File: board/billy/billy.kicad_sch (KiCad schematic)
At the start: 65 parts, among them J1 Screw_Terminal_01x02, J10 Screw_Terminal_01x02, J11 Screw_Terminal_01x02, J2 Conn_01x06, J3 Screw_Terminal_01x02, J4 Screw_Terminal_01x02, J5 USB_C_Receptacle_USB2.0_16P, J6 Screw_Terminal_01x02, J8 Screw_Terminal_01x03, J9 Screw_Terminal_01x02, Q1 AO3400A, Q2 AO3400A, Q3 AO3400A, SW1 TS-1088-AR02016, U1 ESP32-S3-WROOM-1, U2 DRV8833PWP, U3 MAX98357A, U4 DRV8833PWP

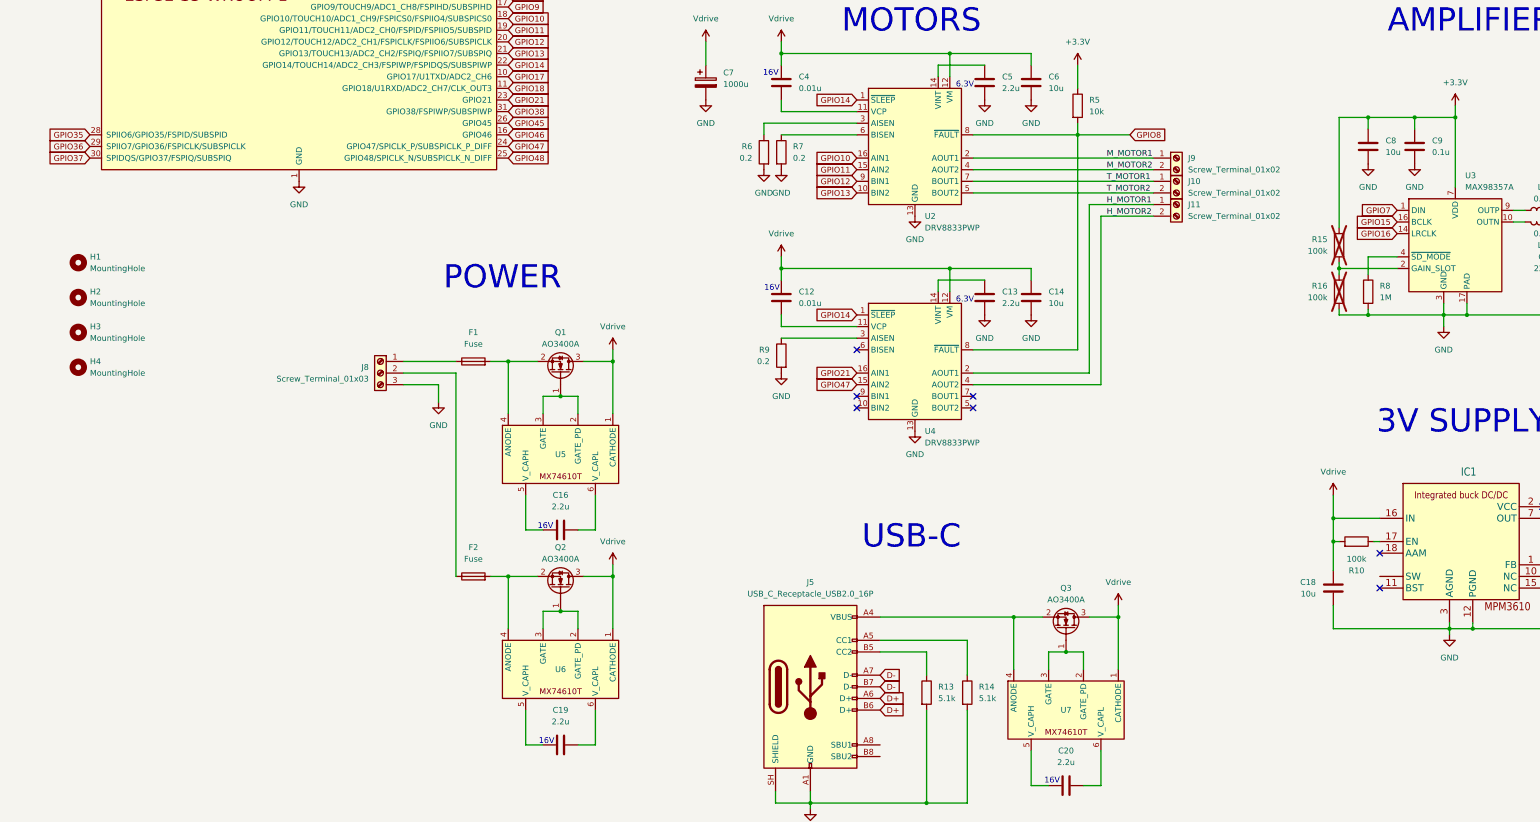
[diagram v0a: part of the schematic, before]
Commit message: Add gated status LED (WS2812, low-side FET VDD switch) to schematic/board and firmware
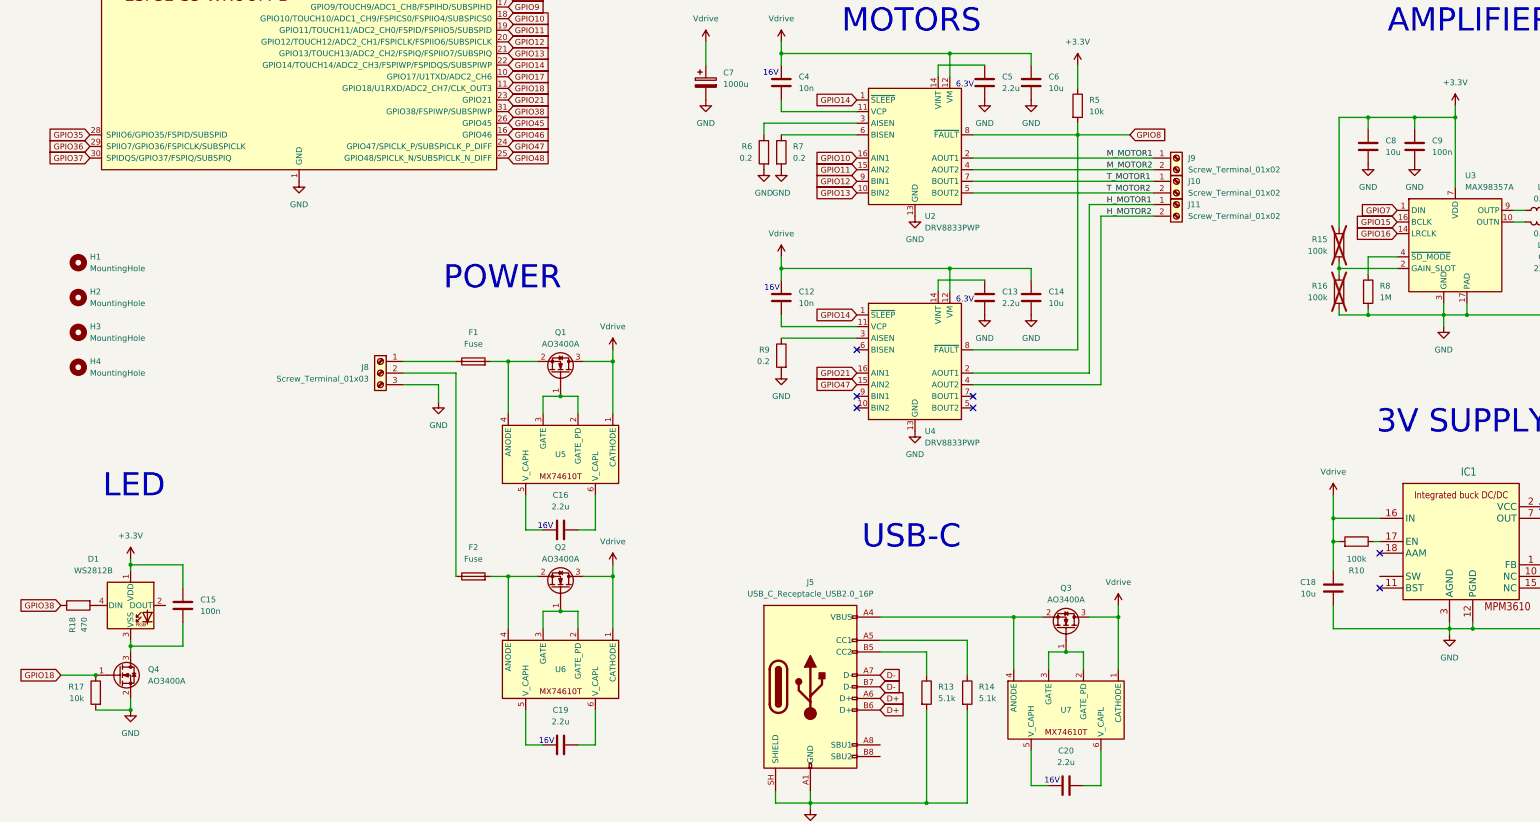
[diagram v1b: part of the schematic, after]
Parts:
- added C15: 100n, Capacitor_SMD:C_0402_1005Metric, symbol Device:C
- added D1: WS2812B, LED_SMD:LED_WS2812B_PLCC4_5.0x5.0mm_P3.2mm, symbol LED:WS2812B
- added Q4: AO3400A, Package_TO_SOT_SMD:SOT-23, symbol Transistor_FET:AO3400A
- added R17: 10k, Resistor_SMD:R_0603_1608Metric, symbol Device:R
- added R18: 470, Resistor_SMD:R_0603_1608Metric, symbol Device:R
- C12, C4: value 0.01u -> 10n
- C9: value 0.1u -> 100n
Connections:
- net +3.3V: now also C15.1, D1.1 (VDD)
- net GND: now also Q4.2 (S), R17.2
- net GPIO18: now also Q4.1 (G), R17.1
- net GPIO38: now also R18.1
- new net: C15.2, D1.3 (VSS), Q4.3 (D)
- new net: D1.4 (DIN), R18.2
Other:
- note added: "LED"

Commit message: Complete board layout, assign LCSC part numbers, verify footprints; passes DRC
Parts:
- C1, C2, C3: footprint Capacitor_SMD:C_0603_1608Metric -> Capacitor_SMD:C_0402_1005Metric; LCSC C15849 -> C52923
- C10, C11: footprint Capacitor_SMD:C_0603_1608Metric -> Capacitor_SMD:C_0402_1005Metric; LCSC C15849 -> C1530
- C16, C19, C20: footprint Capacitor_SMD:C_1206_3216Metric -> Capacitor_SMD:C_0402_1005Metric; LCSC C50254 -> C12530
- J1, J10, J11, J3, J4, J6, J9: LCSC (none) -> C918120
- J2: LCSC (none) -> C56816
- J8: LCSC (none) -> C918121
- L1, L2: value 0.15 -> 50m; LCSC (none) -> C14709
- Q1, Q2, Q3, Q4: LCSC (none) -> AO3400A
- R1, R13, R14: LCSC (none) -> C23186
- R10: LCSC (none) -> C25803
- R11: LCSC (none) -> C23242
- R12: LCSC (none) -> C23352
- R15, R16: now left out of the parts list
- R17, R2, R3, R4, R5: LCSC (none) -> C25804
- R18: LCSC (none) -> C23179
- R6, R7, R9: footprint Resistor_SMD:R_0603_1608Metric -> Resistor_SMD:R_1206_3216Metric; LCSC (none) -> C473037
- R8: LCSC (none) -> C22935
- SW1: footprint billy:SW-SMD_L3.9-W3.0-P4.45 -> Button_Switch_SMD:SW_SPST_TS-1088-xR020; LCSC (none) -> C720477
- U1: LCSC (none) -> C2913203
- U2, U4: value DRV8833PWP -> DRV8833PWPR; LCSC (none) -> C50506
- U3: LCSC (none) -> C910544
- U5, U6, U7: LCSC (none) -> C19078229
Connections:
- no-connect marks 8 -> 12

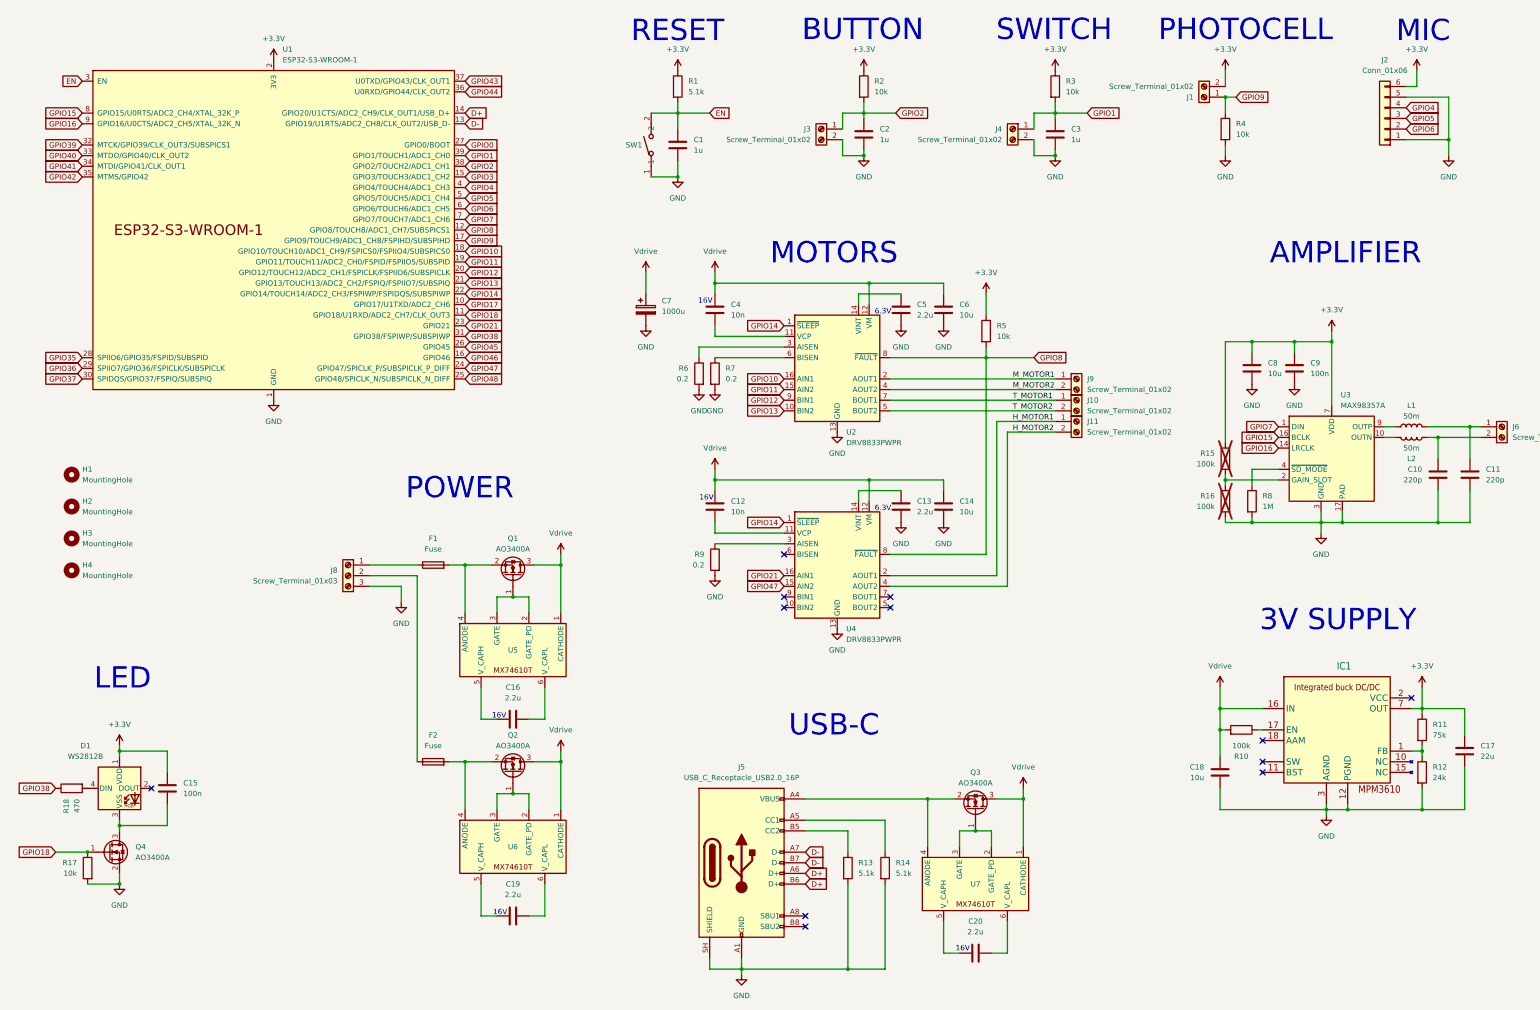
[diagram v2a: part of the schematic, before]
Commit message: Fix some minor ERC and DRC checks
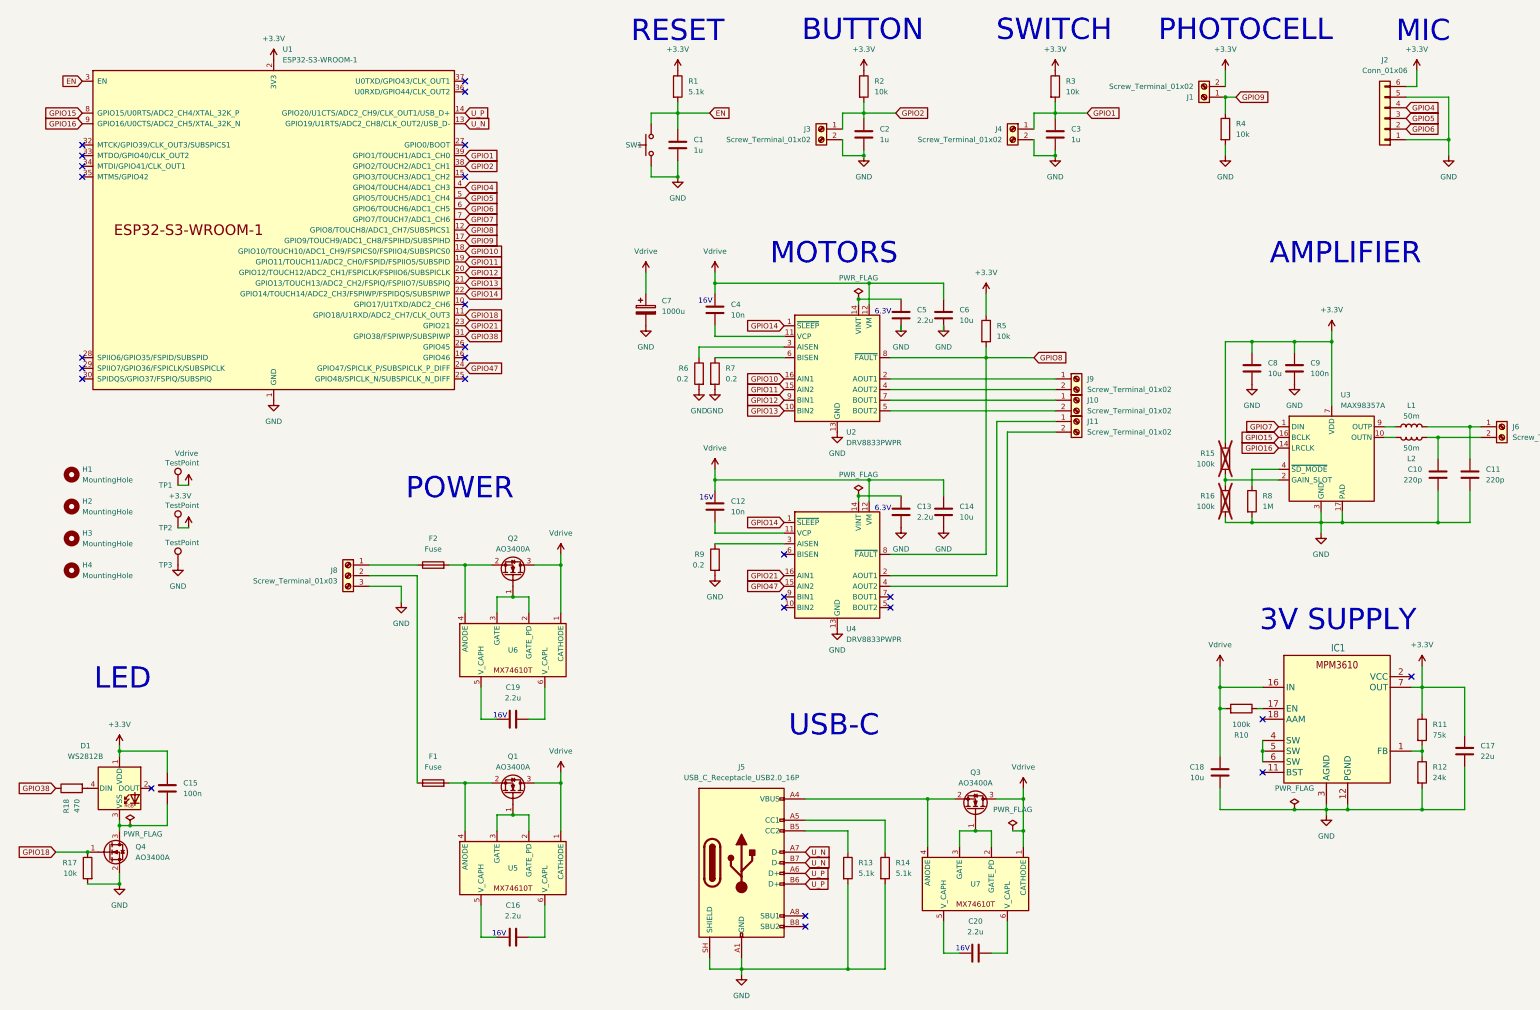
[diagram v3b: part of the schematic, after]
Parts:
- added TP1, TP2, TP3: TestPoint, TestPoint:TestPoint_Pad_1.0x1.0mm, symbol Connector:TestPoint
- SW1: symbol billy:TS-1088-AR02016 -> Switch:SW_Push
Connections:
- net +3.3V: now also TP2.1
- net GND: now also TP3.1
- net Vdrive: now also TP1.1
- net at F1.1: now also J8.2 (Pin_2); no longer J8.1 (Pin_1)
- net at F2.1: now also J8.1 (Pin_1); no longer J8.2 (Pin_2)
- net D+ renamed U_P
- net D- renamed U_N
- net GPIO0: no longer names the net of U1.27 (GPIO0/BOOT)
- net GPIO17: no longer names the net of U1.10 (GPIO17/U1TXD/ADC2_CH6)
- net GPIO3: no longer names the net of U1.15 (GPIO3/TOUCH3/ADC1_CH2)
- net GPIO35: no longer names the net of U1.28 (SPIIO6/GPIO35/FSPID/SUBSPID)
- net GPIO36: no longer names the net of U1.29 (SPIIO7/GPIO36/FSPICLK/SUBSPICLK)
- net GPIO37: no longer names the net of U1.30 (SPIDQS/GPIO37/FSPIQ/SUBSPIQ)
- net GPIO39: no longer names the net of U1.32 (MTCK/GPIO39/CLK_OUT3/SUBSPICS1)
- net GPIO40: no longer names the net of U1.33 (MTDO/GPIO40/CLK_OUT2)
- net GPIO41: no longer names the net of U1.34 (MTDI/GPIO41/CLK_OUT1)
- net GPIO42: no longer names the net of U1.35 (MTMS/GPIO42)
- net GPIO43: no longer names the net of U1.37 (U0TXD/GPIO43/CLK_OUT1)
- net GPIO44: no longer names the net of U1.36 (U0RXD/GPIO44/CLK_OUT2)
- net GPIO45: no longer names the net of U1.26 (GPIO45)
- net GPIO46: no longer names the net of U1.16 (GPIO46)
- net GPIO48: no longer names the net of U1.25 (GPIO48/SPICLK_N/SUBSPICLK_N_DIFF)
- net H_MOTOR1: no longer names the net of J11.1 (Pin_1), U4.2 (AOUT1)
- net H_MOTOR2: no longer names the net of J11.2 (Pin_2), U4.4 (AOUT2)
- net M_MOTOR1: no longer names the net of J9.1 (Pin_1), U2.2 (AOUT1)
- net M_MOTOR2: no longer names the net of J9.2 (Pin_2), U2.4 (AOUT2)
- net T_MOTOR1: no longer names the net of J10.1 (Pin_1), U2.7 (BOUT1)
- net T_MOTOR2: no longer names the net of J10.2 (Pin_2), U2.5 (BOUT2)
- no-connect marks 12 -> 26
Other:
- title: Big Mouth Billy Bass -> Smart Mouth Billy Bass
- moved on the sheet: C13, C14, C16, C19, C5, C6, F1, F2, Q1, Q2, R10, U5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

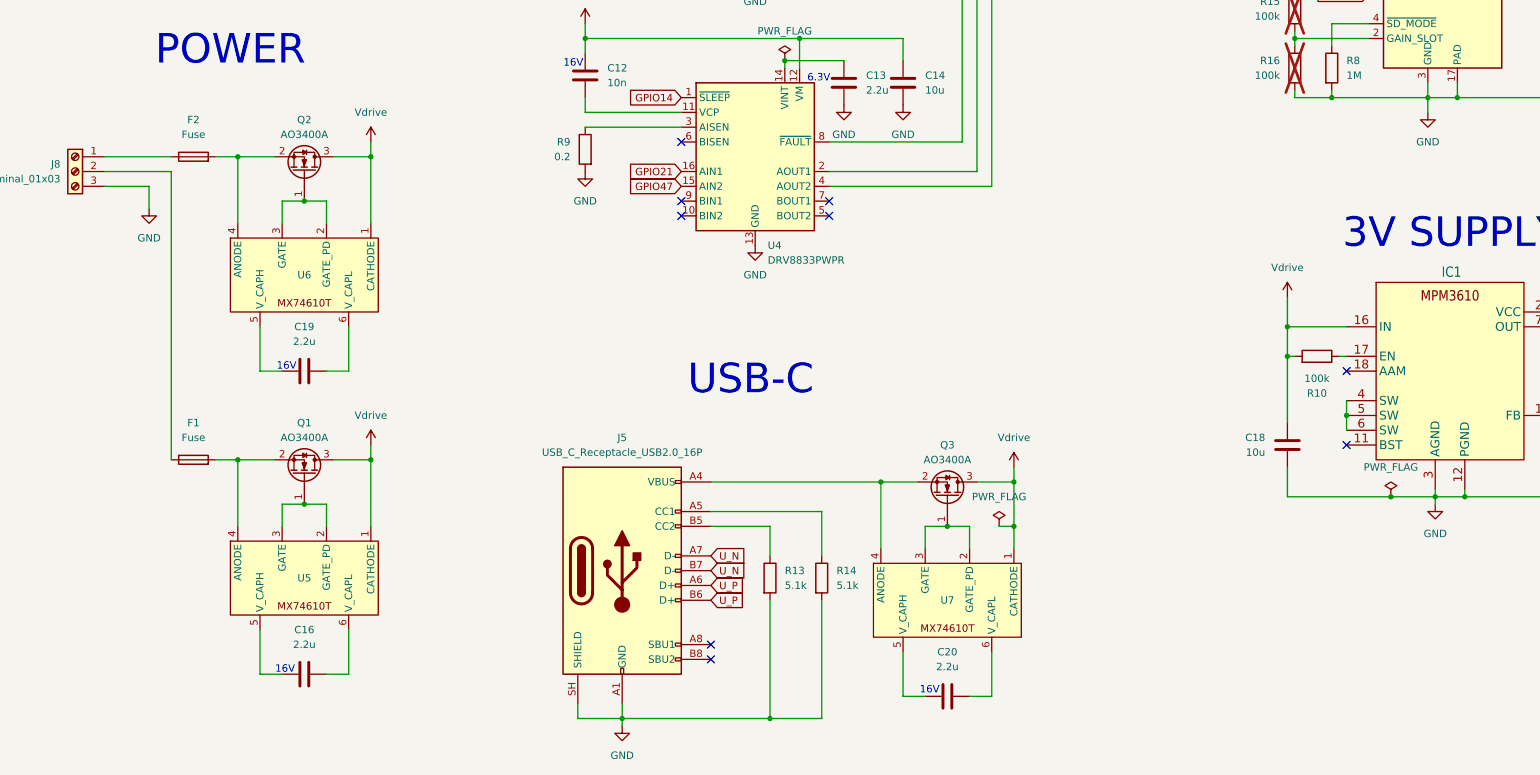
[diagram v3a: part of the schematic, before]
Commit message: Switched to Micro-USB 2.0
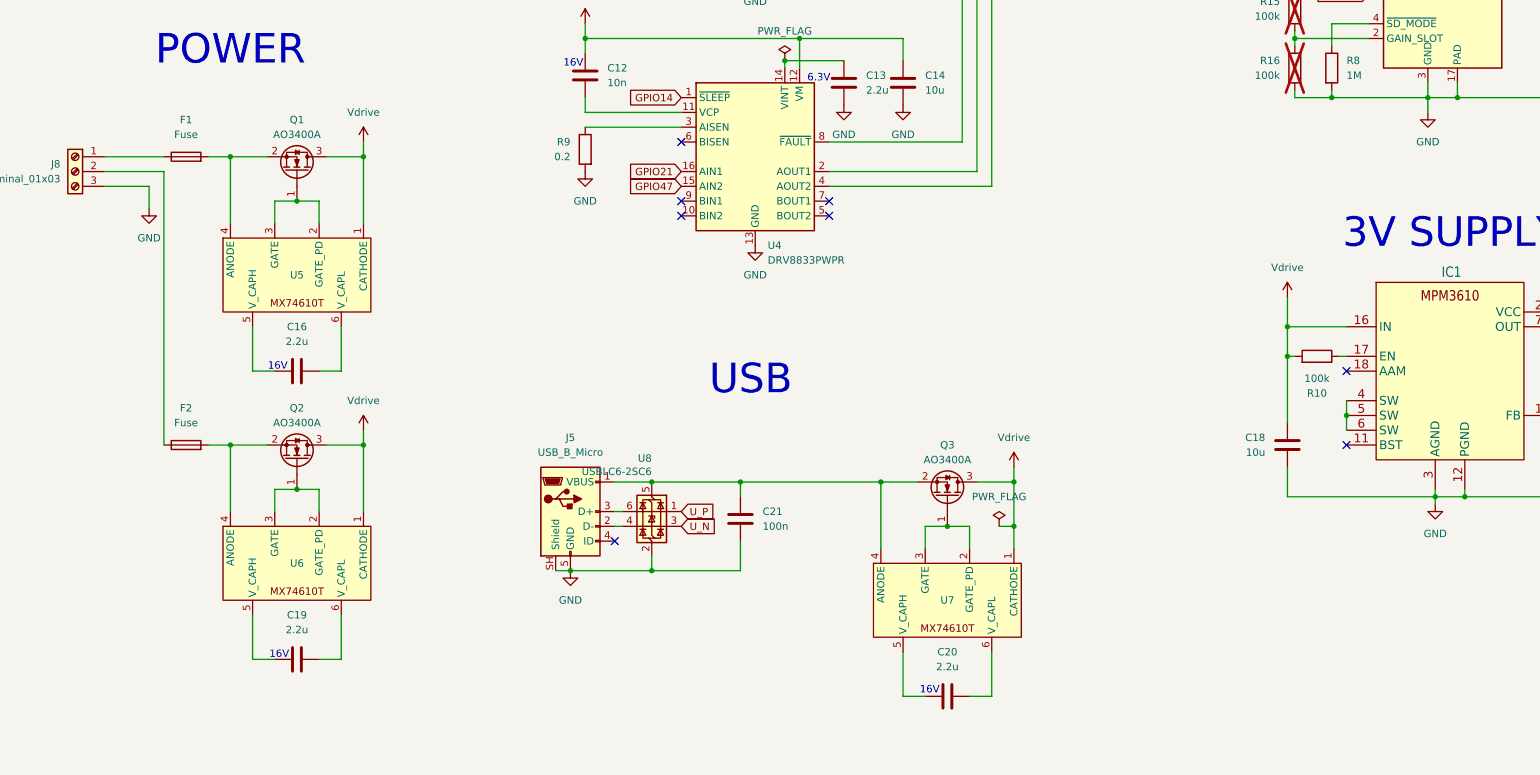
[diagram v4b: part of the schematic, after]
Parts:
- removed J5: USB_C_Receptacle_USB2.0_16P, Connector_USB:USB_C_Receptacle_G-Switch_GT-USB-7010ASV, symbol Connector:USB_C_Receptacle_USB2.0_16P
- removed R13, R14: 5.1k, Resistor_SMD:R_0603_1608Metric, symbol Device:R
- added C21: 100n, Capacitor_SMD:C_0402_1005Metric, symbol Device:C
- added J5: USB_B_Micro, Connector_USB:USB_Micro-B_Amphenol_10118194-0001LF_Horizontal, symbol Connector:USB_B_Micro
- added U8: USBLC6-2SC6, Package_TO_SOT_SMD:SOT-23-6, symbol Power_Protection:USBLC6-2SC6
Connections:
- net GND: now also C21.2, J5.5 (GND), J5.SH (Shield), U8.2 (GND)
- net U_N: now also U8.3 (I/O2)
- net U_P: now also U8.1 (I/O1)
- net at Q3.2 (S), U7.4 (ANODE): now also C21.1, J5.1 (VBUS), U8.5 (VBUS)
- net at F1.1: now also J8.1 (Pin_1); no longer J8.2 (Pin_2)
- net at F2.1: now also J8.2 (Pin_2); no longer J8.1 (Pin_1)
- new net: J5.2 (D-), U8.4 (I/O2)
- new net: J5.3 (D+), U8.6 (I/O1)
- no-connect marks 26 -> 25
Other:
- note added: "USB"
- note removed: "USB-C"
- moved on the sheet: C16, C19, F1, F2, Q1, Q2, U5, U6
